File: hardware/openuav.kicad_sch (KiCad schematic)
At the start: 79 parts, among them J1 Conn_01x01, J10 Conn_01x01, J11 Conn_01x01, J12 Conn_01x01, J13 Conn_01x01, J14 Conn_01x01, J15 Conn_01x01, J16 Conn_01x01, J17 Conn_01x01, J18 Conn_01x01, J19 Conn_01x01, J2 Conn_01x01, J20 Conn_01x01, J21 Conn_01x01, J22 Conn_01x01, J23 Conn_01x01, J24 Conn_01x01, J25 Conn_01x01, J3 Conn_01x01, J4 Conn_01x01, J5 Conn_01x01, J6 Conn_01x01, J7 Conn_01x01, J8 Conn_01x01, J9 Conn_01x01, J99 USB_C_Receptacle_USB2.0, SW1 SW_Push, U1 STM32G431CBUx, U2 LPS22HH, U3 LSM6DSR, U4 TPS54302, U5 TLV75733PDBV, U6 W25N01GVZEIG, U7 TLV75733PDBV

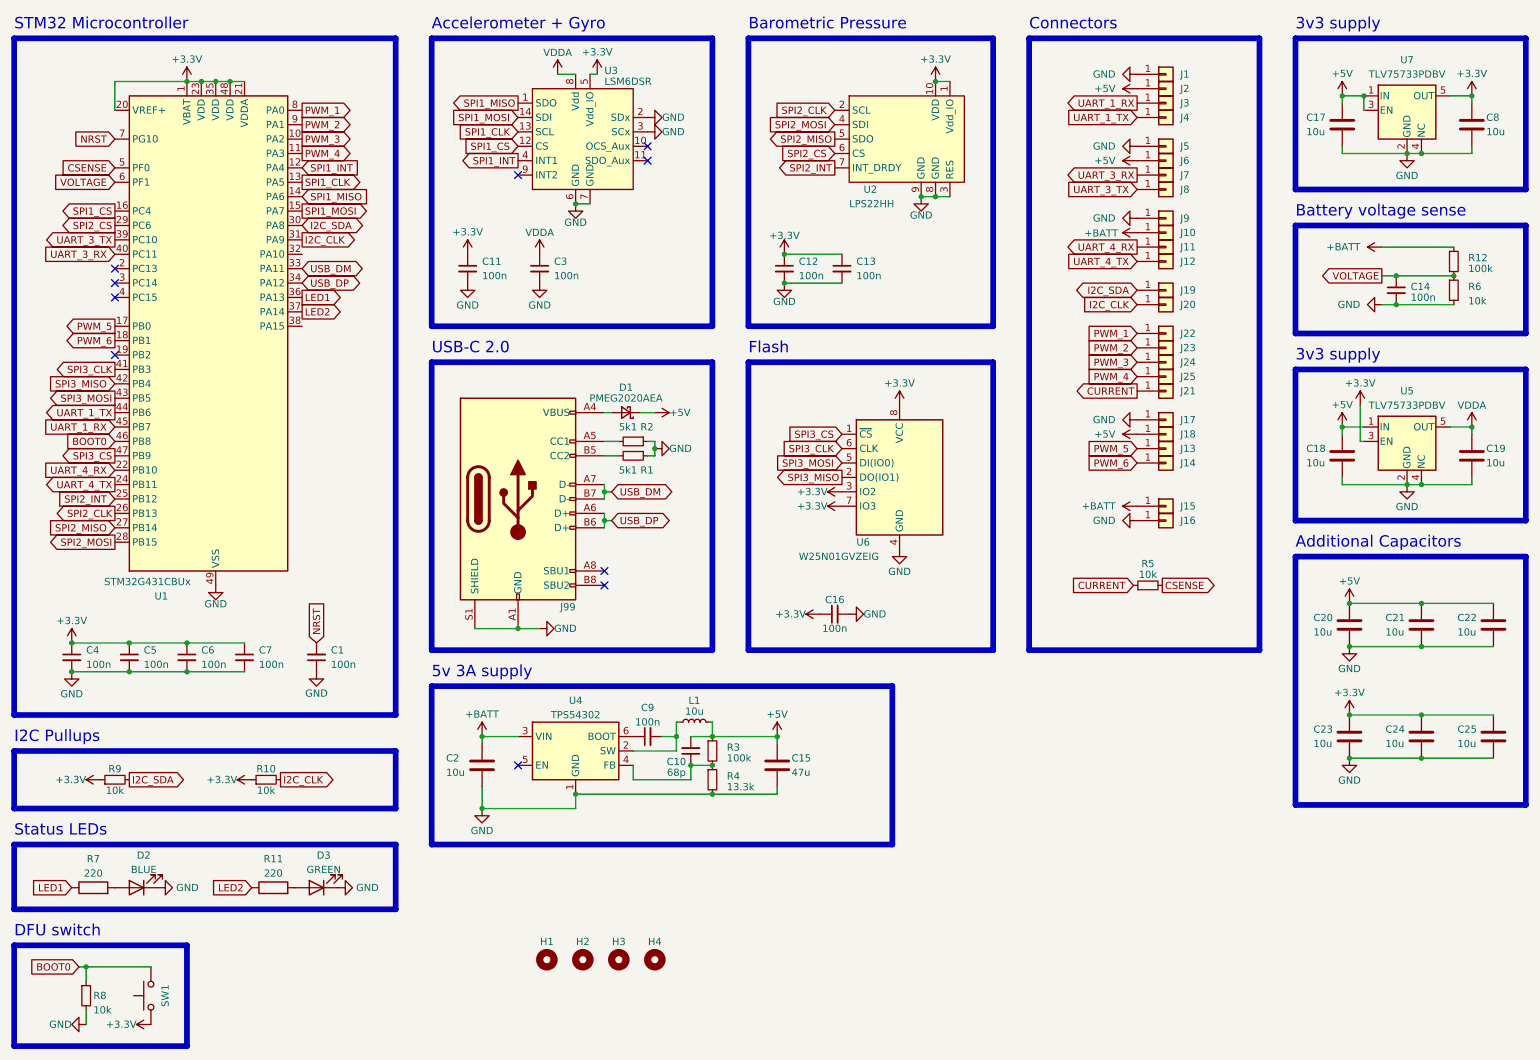
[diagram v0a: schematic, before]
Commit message: Rework supply rail capacitors
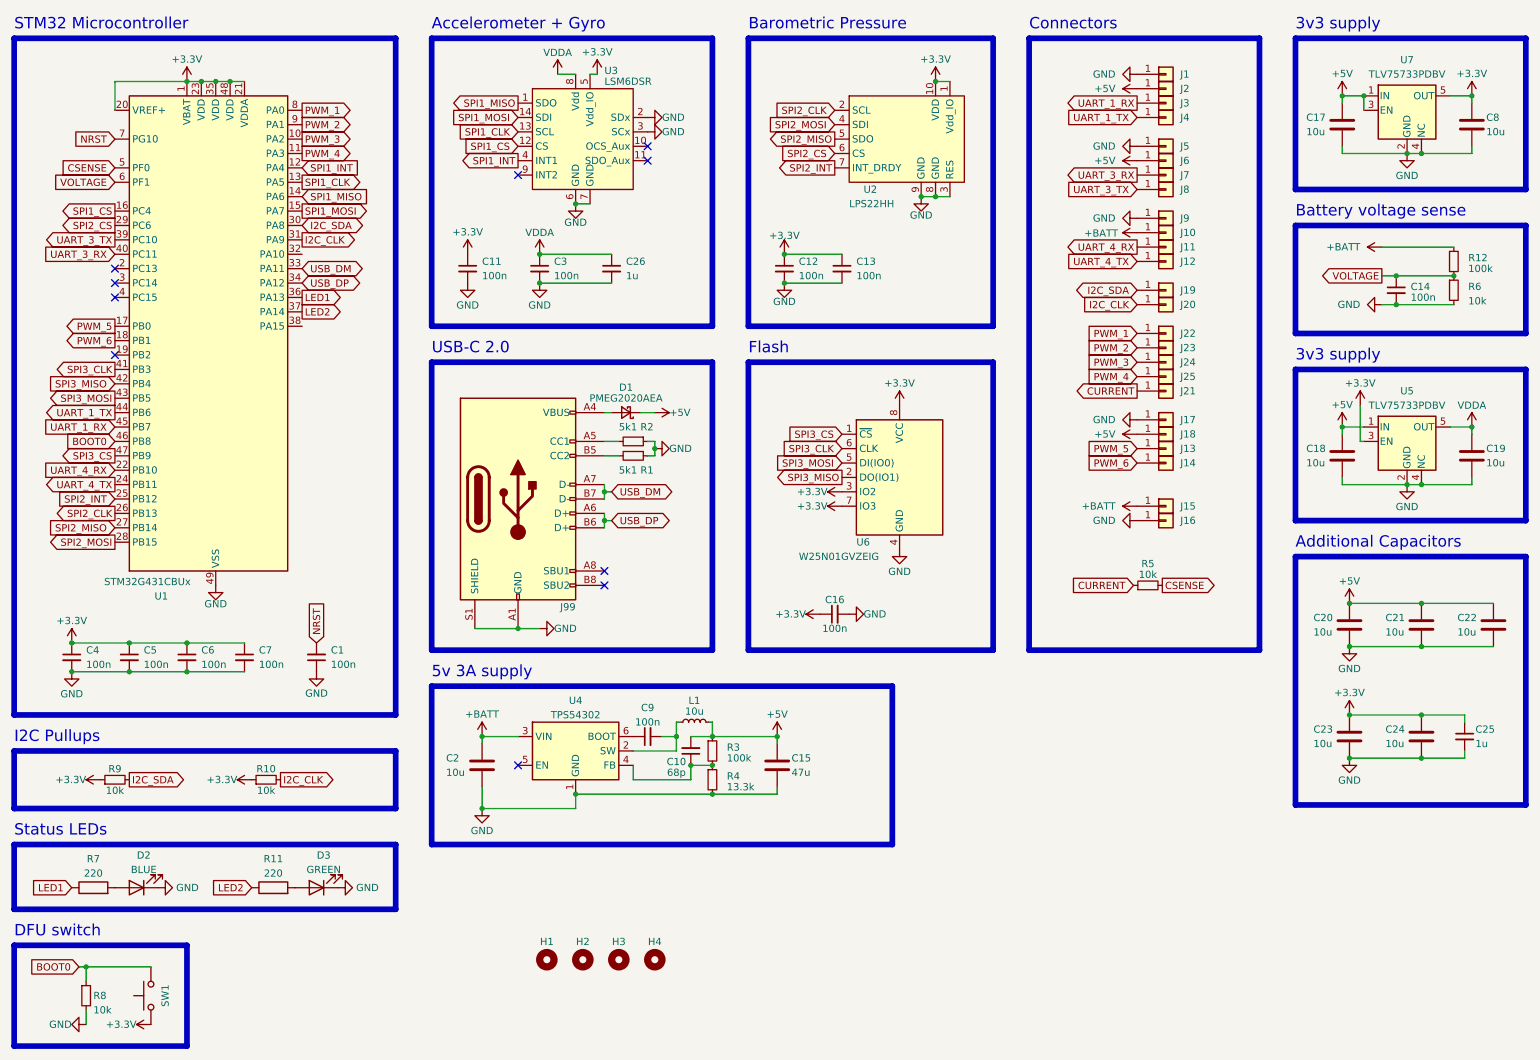
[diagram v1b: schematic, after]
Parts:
- removed C25: 10u, Capacitor_SMD:C_0603_1608Metric, symbol Device:C
- added C25, C26: 1u, Capacitor_SMD:C_0402_1005Metric, symbol Device:C_Small
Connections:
- net +3V3: now also C25.1
- net GND: now also C25.2, C26.2
- net VDDA: now also C26.1
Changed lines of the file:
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@@
   (junction (at 250.825 117.475) (diameter 0) (color 0 0 0 0)
   )
+  (junction (at 107.95 60.96) (diameter 0) (color 0 0 0 0)
+  )
   (junction (at 97.79 153.67) (diameter 0) (color 0 0 0 0)
   )
@@
   (junction (at 253.365 27.94) (diameter 0) (color 0 0 0 0)
   )
+  (junction (at 107.95 55.88) (diameter 0) (color 0 0 0 0)
+  )
   (junction (at 132.08 140.97) (diameter 0) (color 0 0 0 0)
   )
@@
     (stroke (width 0) (type default))
   )
+  (wire (pts (xy 107.95 60.96) (xy 120.65 60.96))
+    (stroke (width 0) (type default))
+  )
+  (wire (pts (xy 271.145 143.51) (xy 271.145 144.78))
+    (stroke (width 0) (type default))
+  )
   (wire (pts (xy 256.54 64.77) (xy 259.08 64.77))
     (stroke (width 0) (type default))
@@
     (stroke (width 0) (type default))
   )
-  (wire (pts (xy 263.525 137.16) (xy 276.225 137.16))
+  (wire (pts (xy 263.525 137.16) (xy 271.145 137.16))
     (stroke (width 0) (type default))
   )
@@
     (stroke (width 0) (type default))
   )
-  (wire (pts (xy 263.525 144.78) (xy 276.225 144.78))
+  (wire (pts (xy 263.525 144.78) (xy 271.145 144.78))
     (stroke (width 0) (type default))
   )
@@
     (stroke (width 0) (type default))
   )
+  (wire (pts (xy 271.145 137.16) (xy 271.145 138.43))
+    (stroke (width 0) (type default))
+  )
   (wire (pts (xy 263.525 117.475) (xy 276.225 117.475))
     (stroke (width 0) (type default))
@@
     (stroke (width 0) (type default))
   )
+  (wire (pts (xy 107.95 55.88) (xy 120.65 55.88))
+    (stroke (width 0) (type default))
+  )
   (wire (pts (xy 272.415 86.36) (xy 272.415 87.63))
     (stroke (width 0) (type default))
@@
     )
   )
-  (symbol (lib_id "Device:C") (at 276.225 140.97 0) (unit 1)
-    (in_bom yes) (on_board yes) (dnp no)
-    (property "Reference" "C25" (at 269.875 139.7 0)
-      (effects (font (size 1.27 1.27)) (justify left))
-    )
-    (property "Value" "10u" (at 269.875 142.24 0)
-      (effects (font (size 1.27 1.27)) (justify left))
-    )
-    (property "Footprint" "Capacitor_SMD:C_0603_1608Metric" (at 277.1902 144.78 0)
-      (effects (font (size 1.27 1.27)) hide)
-    )
-    (property "Datasheet" "~" (at 276.225 140.97 0)
-      (effects (font (size 1.27 1.27)) hide)
-    )
-    (property "LCSC" "C19702" (at 276.225 140.97 0)
-      (effects (font (size 1.27 1.27)) hide)
-    )
-    (pin "1")
-    (pin "2")
-    (instances
-      (project "openuav"
-        (path "/e63e39d7-6ac0-4ffd-8aa3-1841a4541b55"
-          (reference "C25") (unit 1)
-        )
-      )
-    )
-  )
   (symbol (lib_id "power:+5V") (at 149.86 140.97 0) (unit 1)
     (in_bom yes) (on_board yes) (dnp no)
@@
     )
   )
+  (symbol (lib_id "Device:C_Small") (at 120.65 58.42 0) (unit 1)
+    (in_bom yes) (on_board yes) (dnp no) (fields_autoplaced)
+    (property "Reference" "C26" (at 123.19 57.1563 0)
+      (effects (font (size 1.27 1.27)) (justify left))
+    )
+    (property "Value" "1u" (at 123.19 59.6963 0)
+      (effects (font (size 1.27 1.27)) (justify left))
+    )
+    (property "Footprint" "Capacitor_SMD:C_0402_1005Metric" (at 120.65 58.42 0)
+      (effects (font (size 1.27 1.27)) hide)
+    )
+    (property "Datasheet" "~" (at 120.65 58.42 0)
+      (effects (font (size 1.27 1.27)) hide)
+    )
+    (property "LCSC" "C52923" (at 120.65 58.42 0)
+      (effects (font (size 1.27 1.27)) hide)
+    )
+    (pin "1")
+    (pin "2")
+    (instances
+      (project "openuav"
+        (path "/e63e39d7-6ac0-4ffd-8aa3-1841a4541b55"
+          (reference "C26") (unit 1)
+        )
+      )
+    )
+  )
   (symbol (lib_id "Device:C_Small") (at 45.72 127 0) (unit 1)
     (in_bom yes) (on_board yes) (dnp no) (fields_autoplaced)
@@
         )
       )
+    )
+  )
+  (symbol (lib_id "Device:C_Small") (at 271.145 140.97 0) (unit 1)
+    (in_bom yes) (on_board yes) (dnp no)
+    (property "Reference" "C25" (at 273.05 139.7 0)
+      (effects (font (size 1.27 1.27)) (justify left))
+    )
+    (property "Value" "1u" (at 273.05 142.24 0)
+      (effects (font (size 1.27 1.27)) (justify left))
+    )
+    (property "Footprint" "Capacitor_SMD:C_0402_1005Metric" (at 271.145 140.97 0)
+      (effects (font (size 1.27 1.27)) hide)
+    )
+    (property "Datasheet" "~" (at 271.145 140.97 0)
+      (effects (font (size 1.27 1.27)) hide)
+    )
+    (property "LCSC" "C52923" (at 271.145 140.97 0)
+      (effects (font (size 1.27 1.27)) hide)
+    )
+    (pin "1")
+    (pin "2")
+    (instances
+      (project "openuav"
+        (path "/e63e39d7-6ac0-4ffd-8aa3-1841a4541b55"
+          (reference "C25") (unit 1)
+        )
+      )

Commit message: Replace LSM6DSO with LSM6DSR
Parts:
- U3: LCSC C2655100 -> C784817
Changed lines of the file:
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@@
       (effects (font (size 1.27 1.27)) hide)
     )
-    (property "LCSC" "C2655100" (at 115.57 41.91 0)
+    (property "LCSC" "C784817" (at 115.57 41.91 0)
       (effects (font (size 1.27 1.27)) hide)
     )

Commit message: Change IMU to ICM-42688-P. Change top and bottom planes to GND.
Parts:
- U3: value LSM6DSR -> ICM-42688-P; LCSC C784817 -> C1850418
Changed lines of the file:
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@@
       (effects (font (size 1.27 1.27)) (justify left))
     )
-    (property "Value" "LSM6DSR" (at 119.38 25.4 0)
+    (property "Value" "ICM-42688-P" (at 119.38 25.4 0)
       (effects (font (size 1.27 1.27)) (justify left))
     )
@@
       (effects (font (size 1.27 1.27)) hide)
     )
-    (property "LCSC" "C784817" (at 115.57 41.91 0)
+    (property "LCSC" "C1850418" (at 115.57 41.91 0)
       (effects (font (size 1.27 1.27)) hide)
     )

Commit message: Switch buck chip to LMR51420Y, add 9V SMPS.
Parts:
- removed C10: 68p, Capacitor_SMD:C_0402_1005Metric, symbol Device:C_Small
- removed U4: TPS54302, Package_TO_SOT_SMD:SOT-23-6, symbol Regulator_Switching:TPS54302
- added C10: 3.3u, Capacitor_SMD:C_0805_2012Metric, symbol Device:C
- added C27: 100n, Capacitor_SMD:C_0402_1005Metric, symbol Device:C_Small
- added C28: 22u, Capacitor_SMD:C_0805_2012Metric, symbol Device:C
- added L2: 6.8u, Inductor_SMD:L_Sunlord_MWSA0402S, symbol Device:L_Small
- added R13: 309k, Resistor_SMD:R_0402_1005Metric, symbol Device:R_Small
- added R14: 22.1k, Resistor_SMD:R_0402_1005Metric, symbol Device:R_Small
- added U4, U8: ~, Package_TO_SOT_SMD:SOT-23-6, symbol TI_Power:LMR51420
- C15: value 47u -> 22u; footprint Capacitor_SMD:C_1210_3225Metric -> Capacitor_SMD:C_0805_2012Metric; LCSC C77101 -> C45783
- C2: value 10u -> 3.3u; footprint Capacitor_SMD:C_1206_3216Metric -> Capacitor_SMD:C_0805_2012Metric; LCSC C13585 -> C342775
- C20: value 10u -> 22u; footprint Capacitor_SMD:C_0603_1608Metric -> Capacitor_SMD:C_0805_2012Metric; LCSC C19702 -> C45783
- L1: value 10u -> 6.8u; footprint Inductor_SMD:L_Sunlord_MWSA0503S -> Inductor_SMD:L_Sunlord_MWSA0402S; LCSC C408412 -> C408338
- R3: value 100k -> 162k; LCSC C25741 -> (none)
- R4: value 13.3k -> 22.1k; LCSC C274352 -> (none)
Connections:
- net +5V: no longer C20.1
- net +BATT: now also C10.1, U4.3 (VIN), U4.5 (EN), U8.3 (VIN), U8.5 (EN); no longer J10.1 (Pin_1)
- net GND: now also C10.2, C28.2, R14.2, U4.1 (GND), U8.1 (GND)
- net at R3.2, R4.1: now also U8.4 (FB)
- net at L1.1: now also C9.1, U8.2 (SW); no longer C9.2
- new net: C9.2, U8.6 (CB)
- new net: R13.2, R14.1, U4.4 (FB)
- new net: C27.1, L2.1, U4.2 (SW)
- new net: C27.2, U4.6 (CB)
- new net +9V: C20.1, C28.1, J10.1 (Pin_1), L2.2, R13.1
- no-connect marks 10 -> 9
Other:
- note added: "3v3 supply for Gyro"
- note added: "9v 3A supply"
- moved on the sheet: C15, C2, C21, C22, C23, C24, C25, C9, H1, H2, H3, H4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

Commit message: Minor layout improvements and part number changes
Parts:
- D3: LCSC C72043 -> C2986059
- R13: LCSC (none) -> C226980
- R14, R4: LCSC (none) -> C163478
- R3: LCSC (none) -> C185462
- U4, U8: LCSC (none) -> C5383002
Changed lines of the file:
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@@
       (effects (font (size 1.27 1.27)) hide)
     )
+    (property "LCSC" "C5383002" (at 112.395 145.415 0)
+      (effects (font (size 1.27 1.27)) hide)
+    )
     (pin "4")
     (pin "2")
@@
       (effects (font (size 1.27 1.27)) hide)
     )
-    (property "LCSC" "C72043" (at 68.58 167.64 0)
+    (property "LCSC" "C2986059" (at 68.58 167.64 0)
       (effects (font (size 1.27 1.27)) hide)
     )
@@
       (effects (font (size 1.27 1.27)) hide)
     )
+    (property "LCSC" "C163478" (at 131.445 153.035 0)
+      (effects (font (size 1.27 1.27)) hide)
+    )
     (pin "2")
     (pin "1")
@@
       (effects (font (size 1.27 1.27)) hide)
     )
+    (property "LCSC" "C226980" (at 131.445 181.61 0)
+      (effects (font (size 1.27 1.27)) hide)
+    )
     (pin "2")
     (pin "1")
@@
       (effects (font (size 1.27 1.27)) hide)
     )
+    (property "LCSC" "C5383002" (at 112.395 179.07 0)
+      (effects (font (size 1.27 1.27)) hide)
+    )
     (pin "4")
     (pin "2")
@@
       (effects (font (size 1.27 1.27)) hide)
     )
+    (property "LCSC" "C185462" (at 131.445 147.955 0)
+      (effects (font (size 1.27 1.27)) hide)
+    )
     (pin "2")
     (pin "1")
@@
       (effects (font (size 1.27 1.27)) hide)
     )
+    (property "LCSC" "C163478" (at 131.445 186.69 0)
+      (effects (font (size 1.27 1.27)) hide)
+    )
